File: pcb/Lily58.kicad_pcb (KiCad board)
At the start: 2 copper layers, 142.5 x 106.3 mm, 134 parts, among them J2 4PIN, J3 Conn_01x06_Female, J4 Conn_01x06_Female, SW1 SW_PUSH, SW10 SW_PUSH, SW11 SW_PUSH, SW12 SW_PUSH, SW13 SW_PUSH, SW14 SW_PUSH, SW15 SW_PUSH, SW16 SW_PUSH, SW17 SW_PUSH, SW18 SW_PUSH, SW19 SW_PUSH, SW2 SW_PUSH, SW20 SW_PUSH, SW21 SW_PUSH, SW22 SW_PUSH, SW23 SW_PUSH, SW24 SW_PUSH, SW25 SW_PUSH, SW26 SW_PUSH, SW27 SW_PUSH, SW28 SW_PUSH, SW29 SW_PUSH, SW3 SW_PUSH, SW4 SW_PUSH, SW5 SW_PUSH, SW6 SW_PUSH, SW7 SW_PUSH, SW8 SW_PUSH, SW9 SW_PUSH, U1 ProMicro

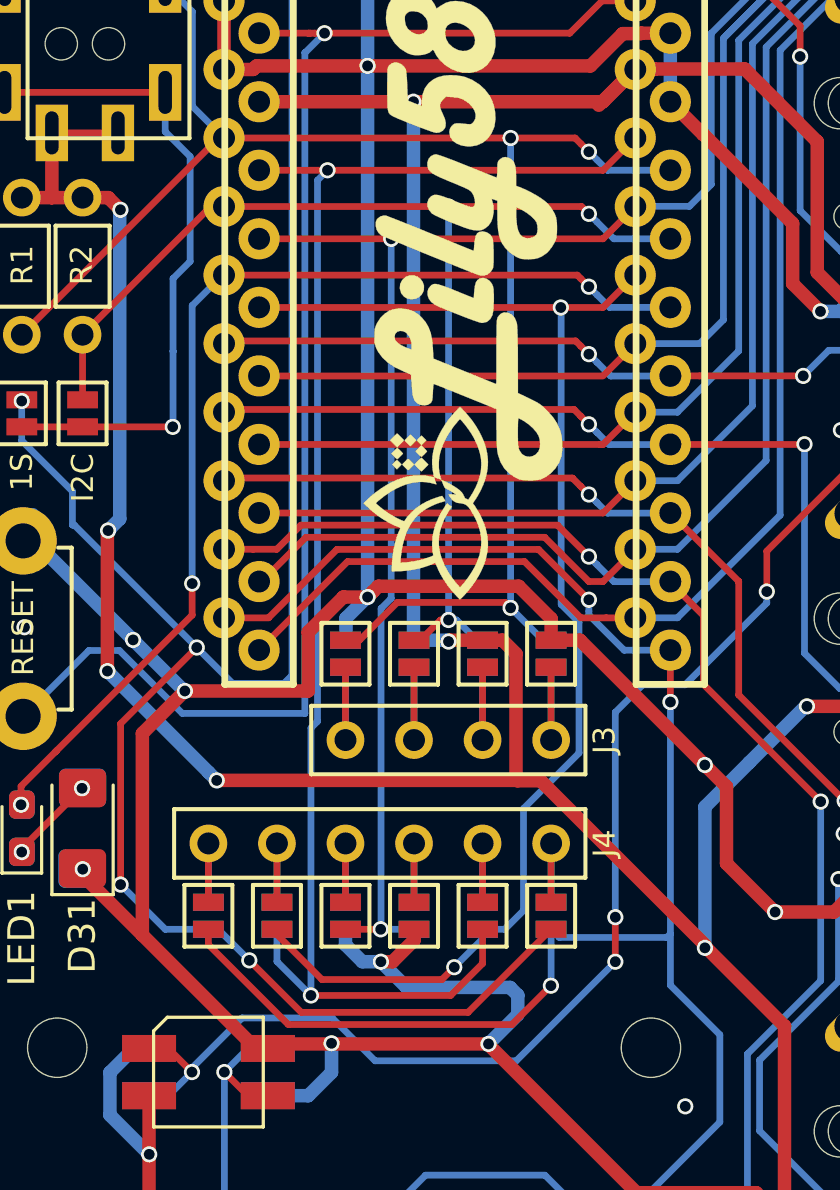
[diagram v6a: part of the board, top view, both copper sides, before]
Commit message: fix joystick pinout
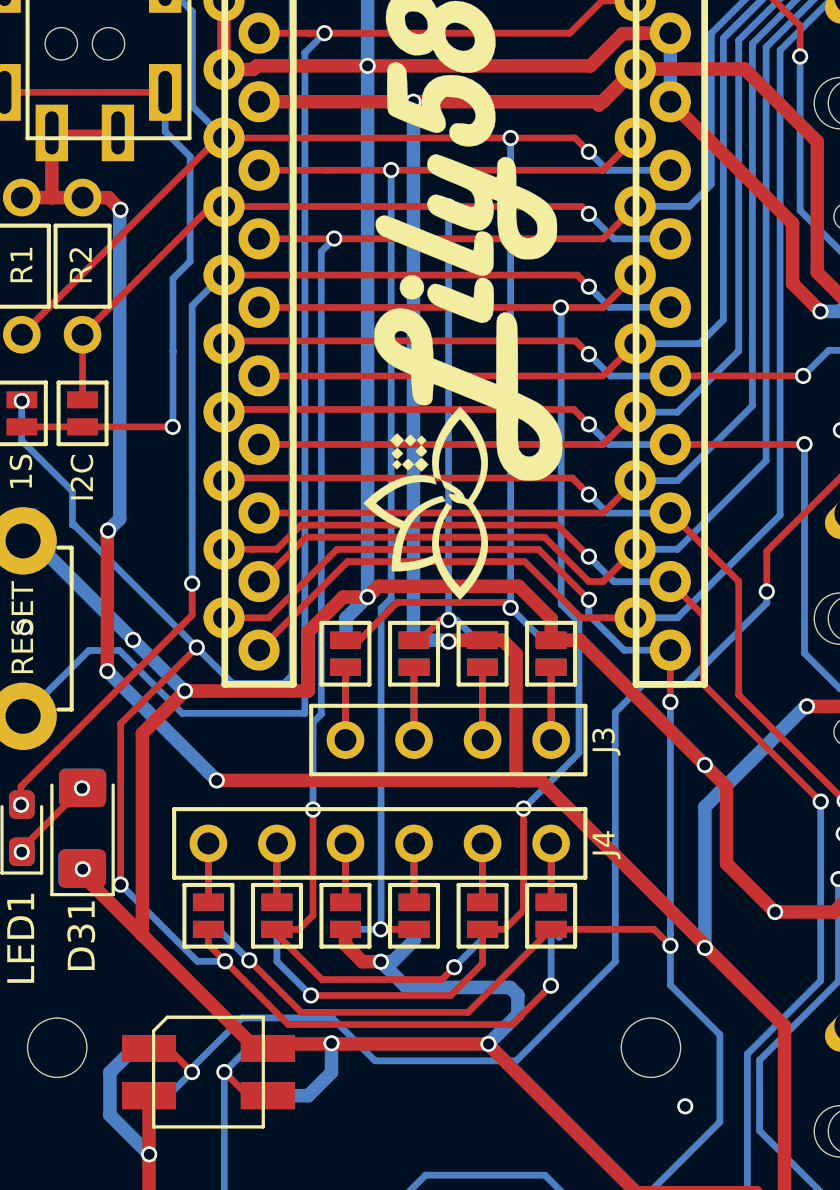
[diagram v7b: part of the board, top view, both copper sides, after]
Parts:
- JP10, JP11, JP12, JP17, JP18, JP9: moved to F.Cu
- JP13, JP14, JP15, JP16, JP19, JP20: moved to B.Cu
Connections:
- JP10 pad 2: A3 -> col0
- JP12 pad 2: col0 -> A3
- JP15 pad 2: col0 -> A3
- JP19 pad 2: A3 -> col0
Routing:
- net A3: track 56.4 -> 45.3 mm
- net col0: track 297.0 -> 305.2 mm, vias 4 -> 5
- net DATA: track 90.2 -> 93.7 mm, vias 6 -> 7
- net row4: track 159.4 -> 157.5 mm, vias 7 -> 8
- net A2: track 49.1 -> 50.7 mm, vias 2 -> 3
- net Net-(D33-Pad3): vias 6 -> 4

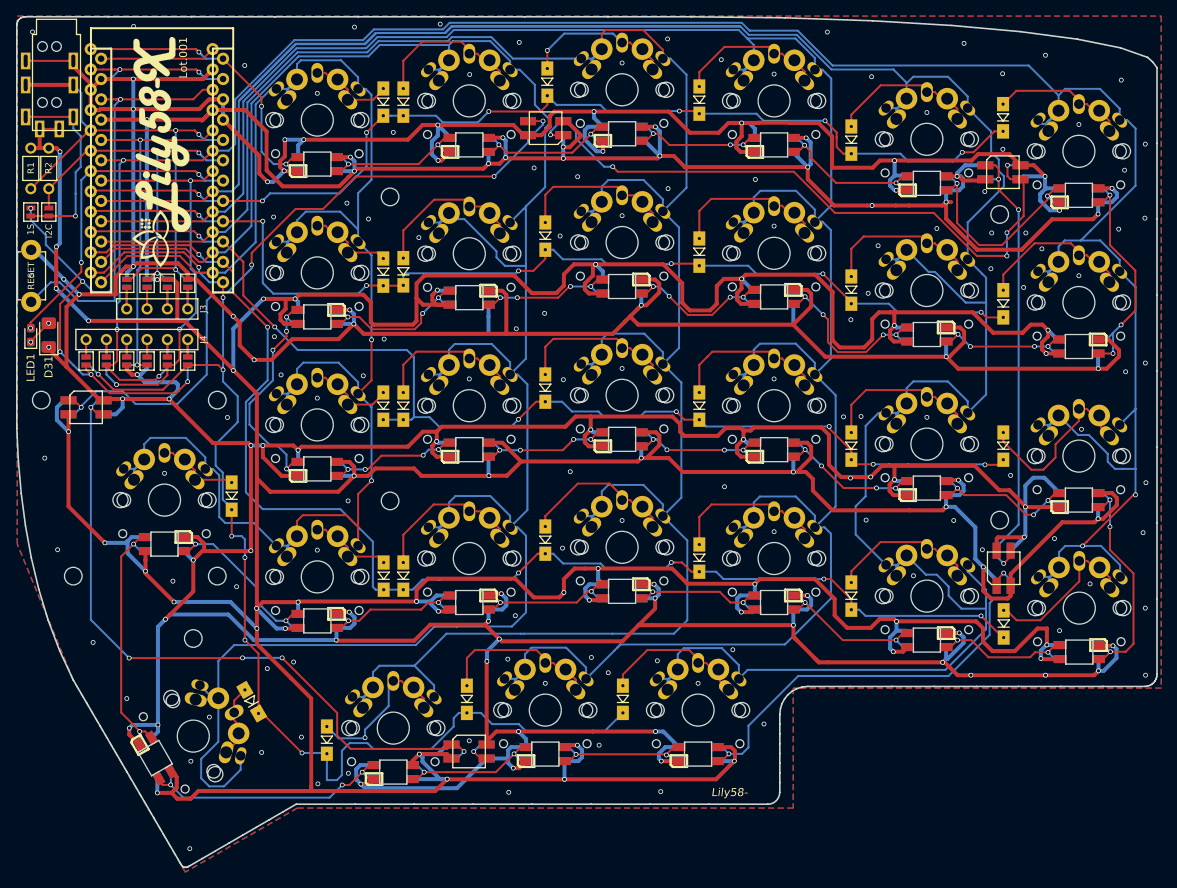
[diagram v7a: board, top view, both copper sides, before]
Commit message: refuctor pcb
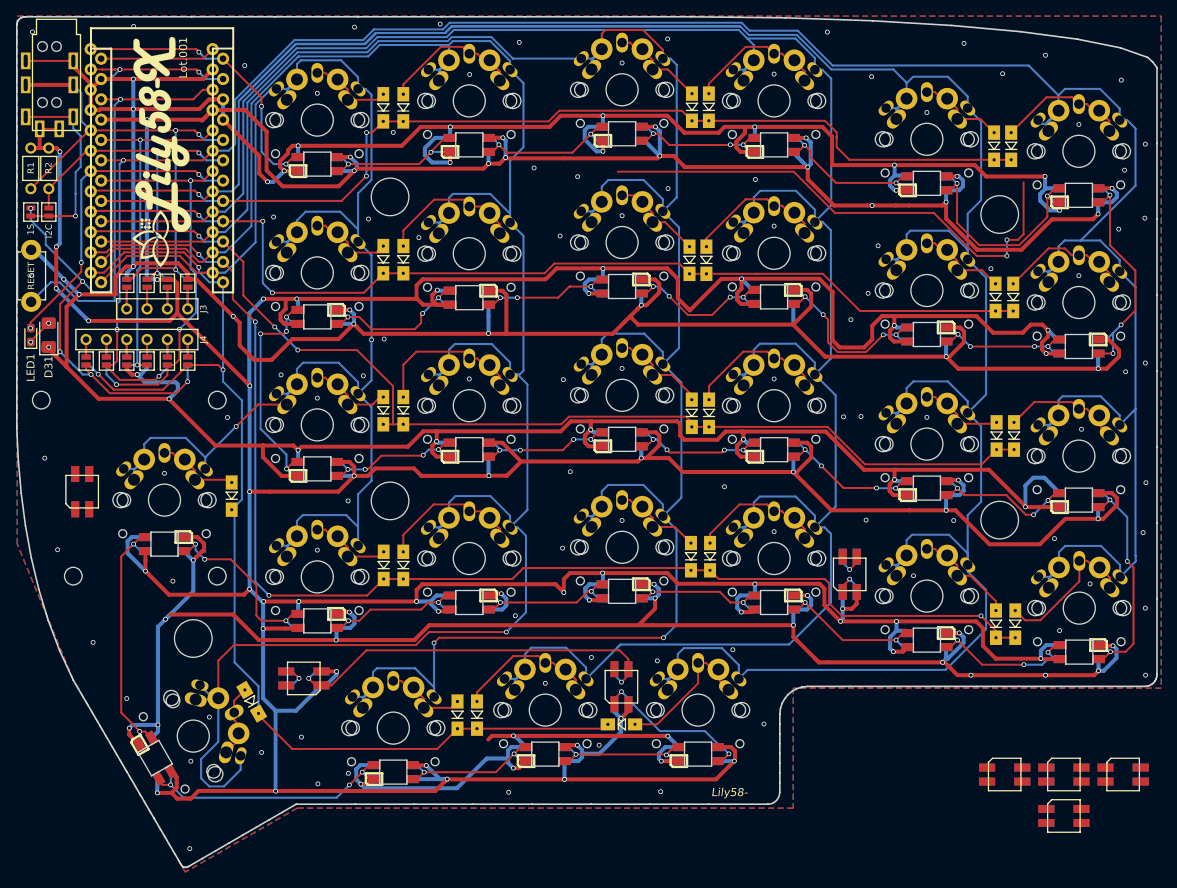
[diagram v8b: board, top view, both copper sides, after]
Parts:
- added D30: SK6812MINI, Lily58-footprint:SK6812MINI_underglow_rev, F.Cu at (206.4, 131.8)
- added D37: SK6812MINI, Lily58-footprint:SK6812MINI_underglow_rev, F.Cu at (213.8, 137.0)
- added D38: SK6812MINI, Lily58-footprint:SK6812MINI_underglow_rev, F.Cu at (221.2, 131.8)
- TH3, TH4, TH5, TH6, TH7: footprint Lily58-footprint:HOLE_M2 -> Lily58-footprint:HOLE_M2_TH
- moved D35 75.7 mm to (213.8, 131.8)
- moved D34 73.6 mm to (91.1, 96.4), turned to 90 degrees
- moved D33 43.5 mm to (118.8, 119.8), turned to 180 degrees
- moved D32 20.7 mm to (158.5, 120.8), turned to 90 degrees
- moved D36 19.3 mm to (187.0, 106.8)
- moved D15 18.6 mm to (167.3, 86.7)
- moved D23 18.4 mm to (205.3, 113.0)
- moved D3 18.4 mm to (167.3, 48.4)
- moved D21 18.3 mm to (167.2, 104.6)
- moved D9 18.3 mm to (167.0, 67.5)
- moved D17 18.2 mm to (205.4, 89.5)
- moved D11 18.1 mm to (205.3, 72.2)
- moved D5 17.9 mm to (205.1, 53.3)
- moved D27 16.6 mm to (138.0, 124.4)
- moved D6 3.70 mm to (207.2, 53.3)
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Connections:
- D33 pad 1: Net-(D32-Pad3) -> Net-(D33-Pad1)
- D33 pad 3: Net-(D33-Pad3) -> Net-(D32-Pad1)
- D34 pad 1: Net-(D33-Pad3) -> Net-(D34-Pad1)
- D34 pad 3: Net-(D34-Pad3) -> Net-(D33-Pad1)
- D35 pad 1: Net-(D34-Pad3) -> Net-(D35-Pad1)
- D35 pad 3: Net-(D35-Pad3) -> Net-(D34-Pad1)
- D36 pad 1: Net-(D35-Pad3) -> Net-(D36-Pad1)
- D36 pad 3: Net-(D36-Pad3) -> Net-(D35-Pad1)
- L29 pad 1: Net-(D36-Pad3) -> Net-(D32-Pad3)
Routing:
- net Net-(D33-Pad3): track 87.1 -> 0.00 mm, vias 4 -> 0
- net GND: track 1028.8 -> 960.0 mm, vias 181 -> 149
- net Net-(D32-Pad3): track 88.1 -> 21.2 mm, vias 5 -> 2
- net VCC: track 1064.1 -> 999.3 mm
- net Net-(D35-Pad3): track 57.4 -> 0.00 mm, vias 3 -> 0
- net Net-(D36-Pad3): track 55.4 -> 0.00 mm, vias 2 -> 0
- net Net-(D32-Pad1): track 3.92 -> 50.6 mm, vias 1 -> 2
- net Net-(D34-Pad3): track 82.5 -> 63.9 mm, vias 5 -> 2
- net row4: track 157.5 -> 143.8 mm, vias 8 -> 3
- net Net-(D27-Pad2): track 20.9 -> 12.3 mm, vias 1 -> 0
- net Net-(D17-Pad2): track 20.3 -> 11.9 mm
- net Net-(D9-Pad2): track 20.1 -> 12.3 mm
- net Net-(D15-Pad2): track 20.2 -> 12.4 mm
- net Net-(D11-Pad2): track 20.1 -> 12.4 mm
- net Net-(D21-Pad2): track 19.7 -> 12.1 mm
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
